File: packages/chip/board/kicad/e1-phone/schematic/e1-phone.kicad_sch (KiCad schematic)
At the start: 0 parts

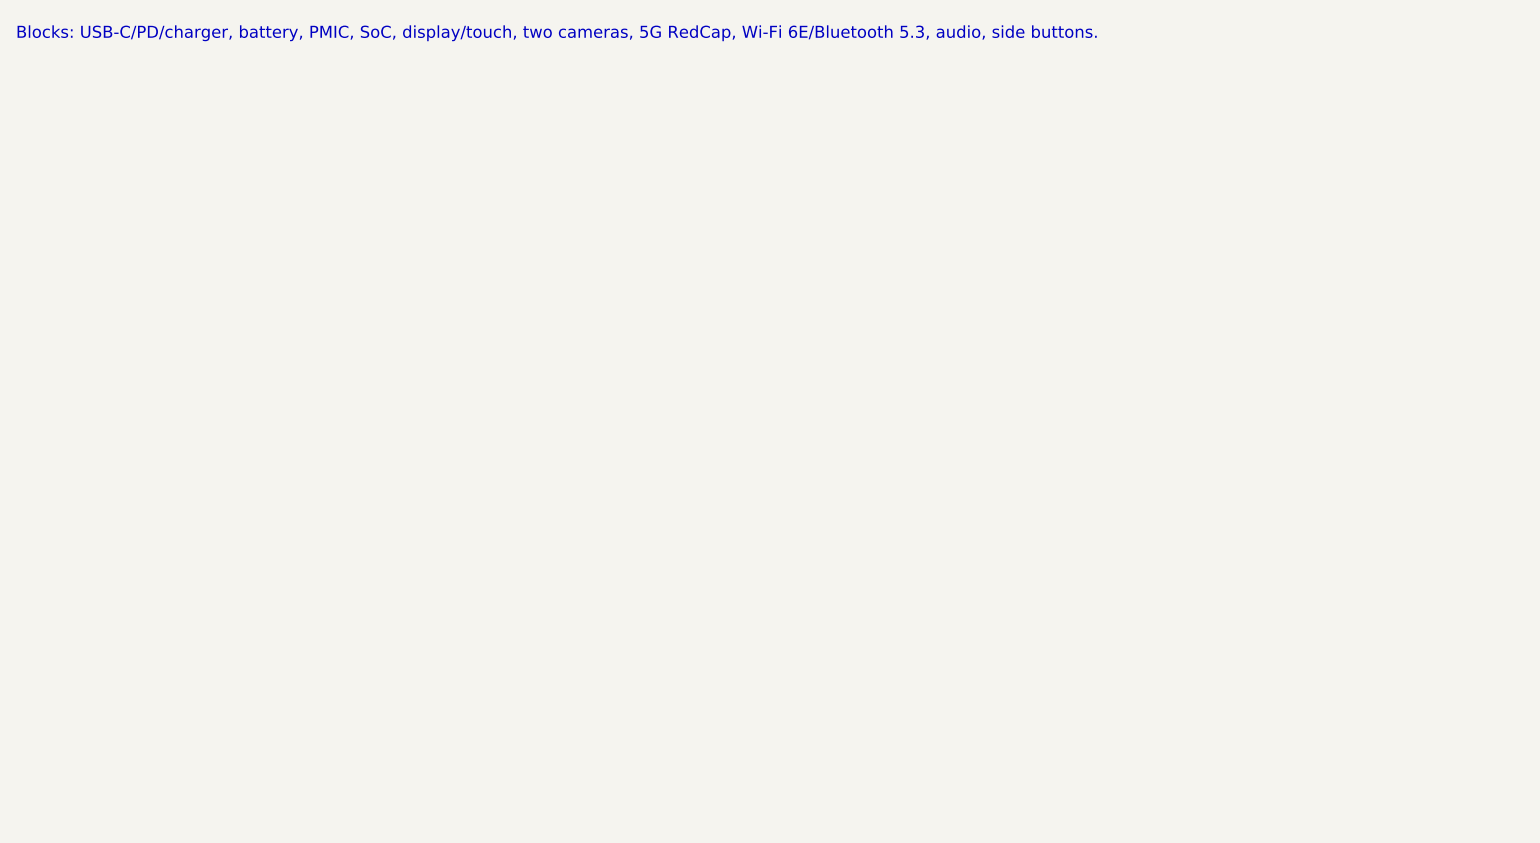
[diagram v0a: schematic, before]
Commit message: Prepare chip package for publishing
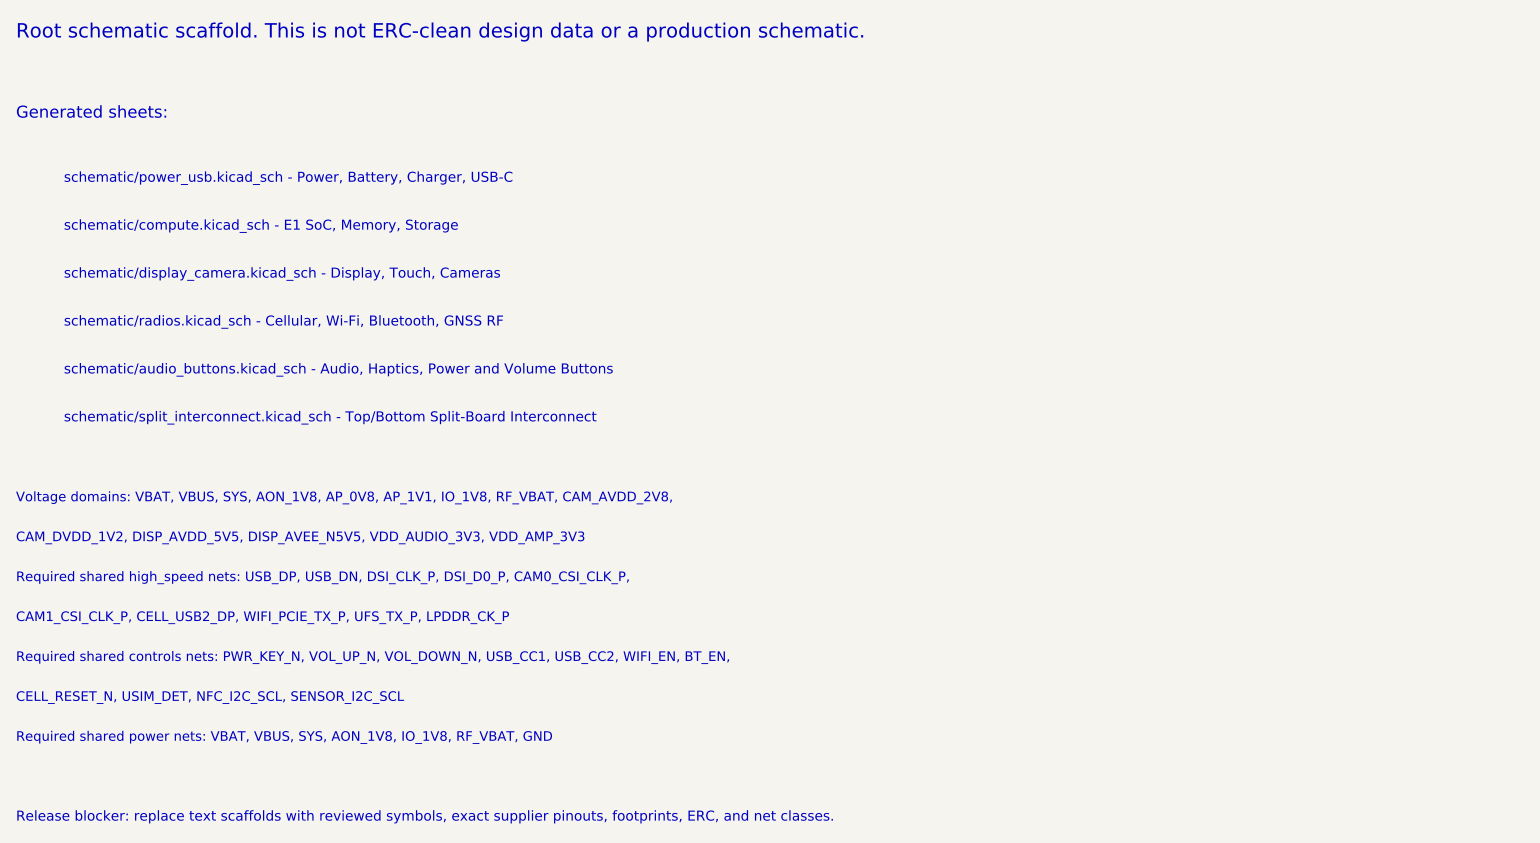
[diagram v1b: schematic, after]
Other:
- note added: "CAM1_CSI_CLK_P, CELL_USB2_DP, WIFI_PCIE_TX_P, UFS_TX_P, LPDDR_CK_P"
- note added: "CAM_DVDD_1V2, DISP_AVDD_5V5, DISP_AVEE_N5V5, VDD_AUDIO_3V3, VDD_AMP_3V3"
- note added: "CELL_RESET_N, USIM_DET, NFC_I2C_SCL, SENSOR_I2C_SCL"
- note added: "Generated sheets:"
- note added: "Release blocker: replace text scaffolds with reviewed symbols, exact supplier pinouts, footprints, ERC, and net classes."
- note added: "Required shared controls nets: PWR_KEY_N, VOL_UP_N, VOL_DOWN_N, USB_CC1, USB_CC2, WIFI_EN, BT_EN,"
- note added: "Required shared high_speed nets: USB_DP, USB_DN, DSI_CLK_P, DSI_D0_P, CAM0_CSI_CLK_P,"
- note added: "Required shared power nets: VBAT, VBUS, SYS, AON_1V8, IO_1V8, RF_VBAT, GND"
- note added: "Root schematic scaffold. This is not ERC-clean design data or a production schematic."
- note added: "Voltage domains: VBAT, VBUS, SYS, AON_1V8, AP_0V8, AP_1V1, IO_1V8, RF_VBAT, CAM_AVDD_2V8,"
- note added: "schematic/audio_buttons.kicad_sch - Audio, Haptics, Power and Volume Buttons"
- note added: "schematic/compute.kicad_sch - E1 SoC, Memory, Storage"
- note added: "schematic/display_camera.kicad_sch - Display, Touch, Cameras"
- note added: "schematic/power_usb.kicad_sch - Power, Battery, Charger, USB-C"
- note added: "schematic/radios.kicad_sch - Cellular, Wi-Fi, Bluetooth, GNSS RF"
- note added: "schematic/split_interconnect.kicad_sch - Top/Bottom Split-Board Interconnect"
- note removed: "Blocks: USB-C/PD/charger, battery, PMIC, SoC, display/touch, two cameras, 5G RedCap, Wi-Fi 6E/Bluetooth 5.3, audio, side buttons."
- company: Eliza local planning scaffold -> Eliza phone board planning
- title: Eliza E1 Phone Mainboard - planning schematic -> E1 Phone Mainboard - schematic scaffold
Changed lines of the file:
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@@
-(kicad_sch (version 20230121) (generator "eliza-phone-scaffold")
+(kicad_sch (version 20230121) (generator "eliza-phone-netlist-scaffold")
   (paper "A3")
   (title_block
-    (title "Eliza E1 Phone Mainboard - planning schematic")
+    (title "E1 Phone Mainboard - schematic scaffold")
     (date "2026-05-20")
-    (rev "EVT0-concept")
-    (company "Eliza local planning scaffold")
-    (comment 1 "Non-release scaffold: supplier pinouts, ERC, DRC, Gerbers, and STEP missing")
+    (rev "concept-netlist-r0")
+    (company "Eliza phone board planning")
+    (comment 1 "Evidence class: non_release_schematic_scaffold")
+    (comment 2 "Display anchor: 5.5 inch 1080x1920 MIPI, board 64 x 132 mm")
+    (comment 3 "Source: block-netlist.yaml and routing-constraints.yaml")
   )
-  (text "Blocks: USB-C/PD/charger, battery, PMIC, SoC, display/touch, two cameras, 5G RedCap, Wi-Fi 6E/Bluetooth 5.3, audio, side buttons." (at 20 20 0)
-    (effects (font (size 1.5 1.5)) (justify left bottom))
+  (text "Root schematic scaffold. This is not ERC-clean design data or a production schematic." (at 20.00 20.00 0)
+    (effects (font (size 1.80 1.80)) (justify left bottom))
+  )
+  (text "Generated sheets:" (at 20.00 30.00 0)
+    (effects (font (size 1.50 1.50)) (justify left bottom))
+  )
+  (text "schematic/power_usb.kicad_sch - Power, Battery, Charger, USB-C" (at 26.00 38.00 0)
+    (effects (font (size 1.25 1.25)) (justify left bottom))
+  )
+  (text "schematic/compute.kicad_sch - E1 SoC, Memory, Storage" (at 26.00 44.00 0)
+    (effects (font (size 1.25 1.25)) (justify left bottom))
+  )
+  (text "schematic/display_camera.kicad_sch - Display, Touch, Cameras" (at 26.00 50.00 0)
+    (effects (font (size 1.25 1.25)) (justify left bottom))
+  )
+  (text "schematic/radios.kicad_sch - Cellular, Wi-Fi, Bluetooth, GNSS RF" (at 26.00 56.00 0)
+    (effects (font (size 1.25 1.25)) (justify left bottom))
+  )
+  (text "schematic/audio_buttons.kicad_sch - Audio, Haptics, Power and Volume Buttons" (at 26.00 62.00 0)
+    (effects (font (size 1.25 1.25)) (justify left bottom))
+  )
+  (text "schematic/split_interconnect.kicad_sch - Top/Bottom Split-Board Interconnect" (at 26.00 68.00 0)
+    (effects (font (size 1.25 1.25)) (justify left bottom))
+  )
+  (text "Voltage domains: VBAT, VBUS, SYS, AON_1V8, AP_0V8, AP_1V1, IO_1V8, RF_VBAT, CAM_AVDD_2V8," (at 20.00 78.00 0)
+    (effects (font (size 1.20 1.20)) (justify left bottom))
+  )
+  (text "CAM_DVDD_1V2, DISP_AVDD_5V5, DISP_AVEE_N5V5, VDD_AUDIO_3V3, VDD_AMP_3V3" (at 20.00 83.00 0)
+    (effects (font (size 1.20 1.20)) (justify left bottom))
+  )
+  (text "Required shared high_speed nets: USB_DP, USB_DN, DSI_CLK_P, DSI_D0_P, CAM0_CSI_CLK_P," (at 20.00 88.00 0)
+    (effects (font (size 1.20 1.20)) (justify left bottom))
+  )
+  (text "CAM1_CSI_CLK_P, CELL_USB2_DP, WIFI_PCIE_TX_P, UFS_TX_P, LPDDR_CK_P" (at 20.00 93.00 0)
+    (effects (font (size 1.20 1.20)) (justify left bottom))
+  )
+  (text "Required shared controls nets: PWR_KEY_N, VOL_UP_N, VOL_DOWN_N, USB_CC1, USB_CC2, WIFI_EN, BT_EN," (at 20.00 98.00 0)
+    (effects (font (size 1.20 1.20)) (justify left bottom))
+  )
+  (text "CELL_RESET_N, USIM_DET, NFC_I2C_SCL, SENSOR_I2C_SCL" (at 20.00 103.00 0)
+    (effects (font (size 1.20 1.20)) (justify left bottom))
+  )
+  (text "Required shared power nets: VBAT, VBUS, SYS, AON_1V8, IO_1V8, RF_VBAT, GND" (at 20.00 108.00 0)
+    (effects (font (size 1.20 1.20)) (justify left bottom))
+  )
+  (text "Release blocker: replace text scaffolds with reviewed symbols, exact supplier pinouts, footprints, ERC, and net classes." (at 20.00 118.00 0)
+    (effects (font (size 1.25 1.25)) (justify left bottom))
   )
 )
